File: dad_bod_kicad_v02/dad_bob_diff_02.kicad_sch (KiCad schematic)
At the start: 68 parts

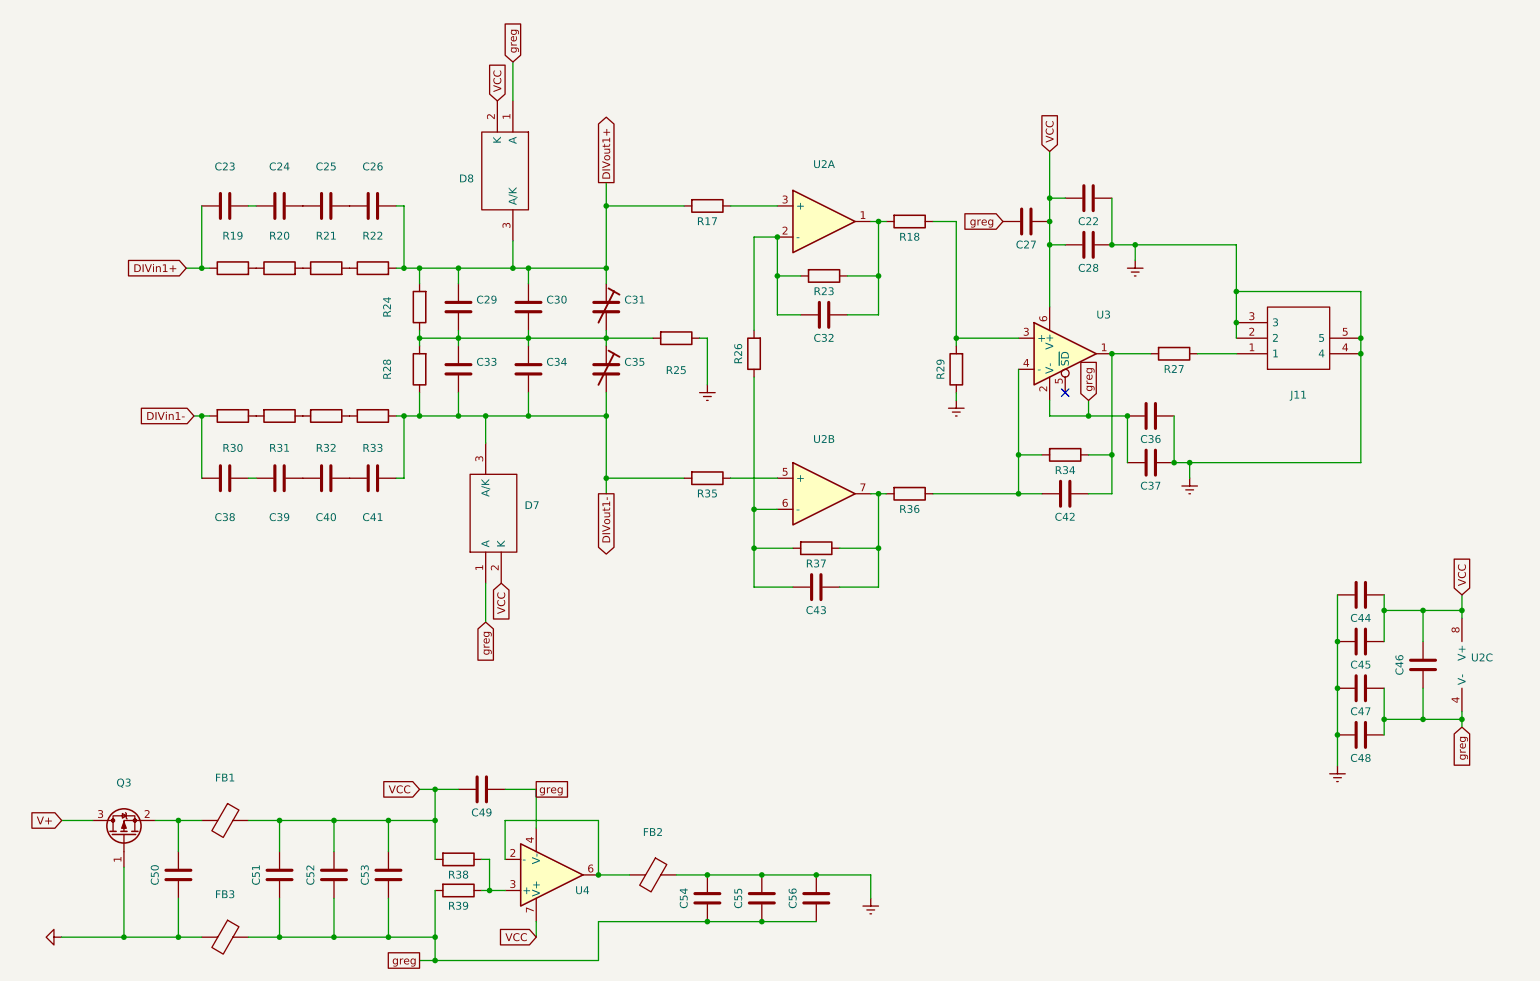
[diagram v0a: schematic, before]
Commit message: Added BOMs & db_standalone order
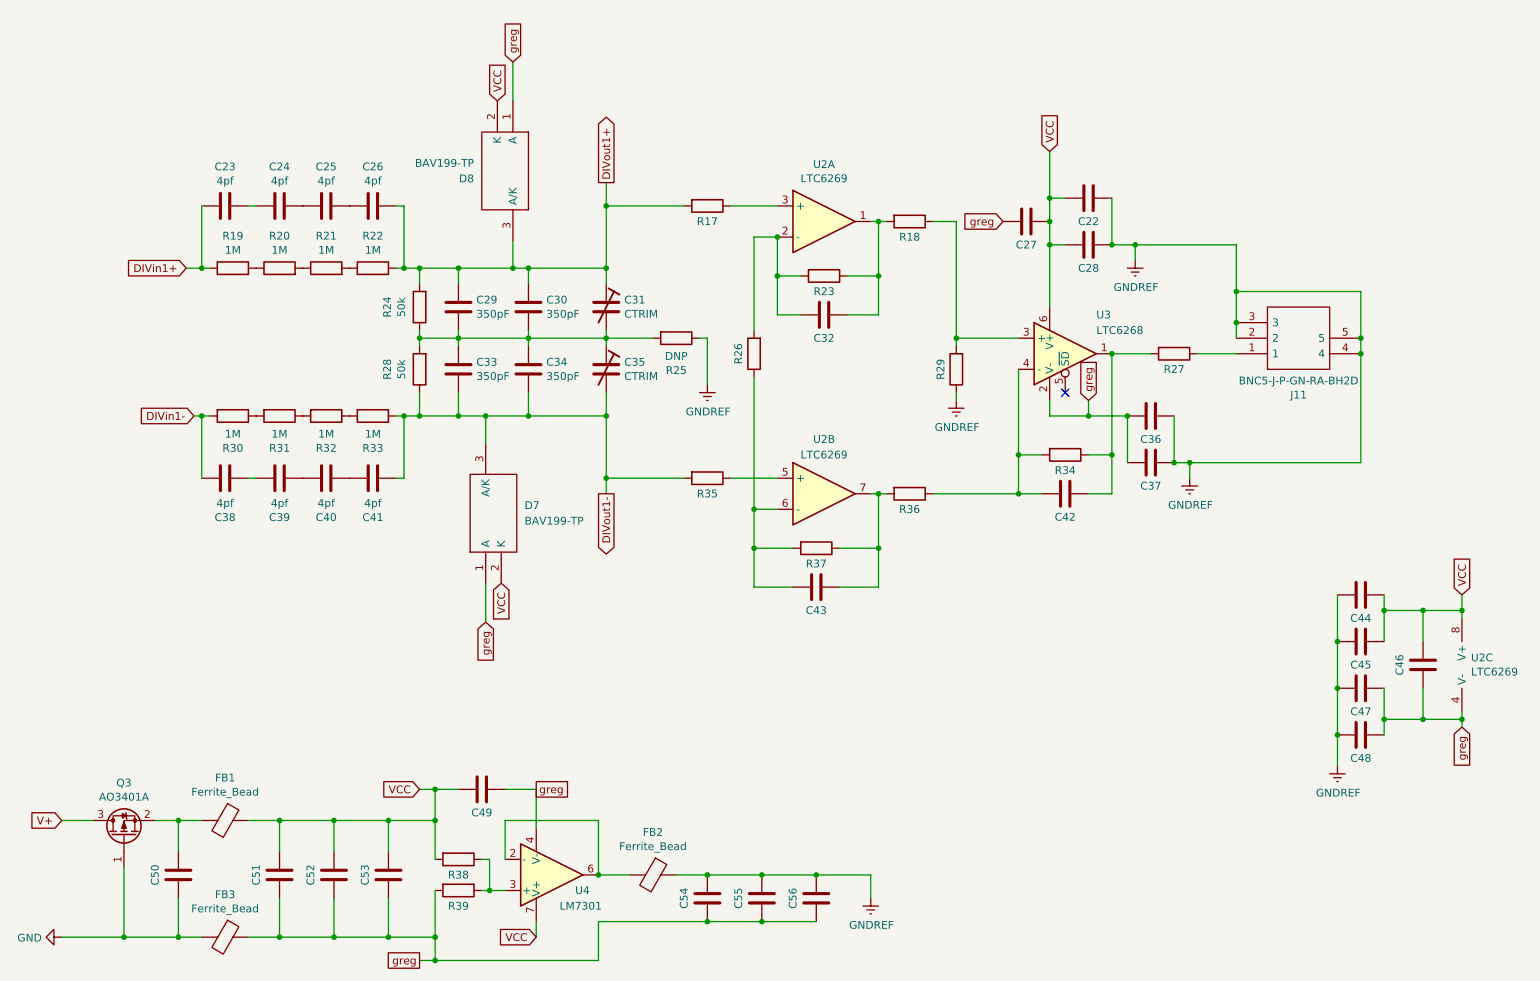
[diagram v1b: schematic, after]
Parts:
- C22, C27, C28, C32, C36, C37, C42, C43, C44, C45, C46, C47, C48, C49, C50, C51, C52, C53, C54, C55, C56: value (none) -> ~; footprint (none) -> Capacitor_SMD:C_0805_2012Metric_Pad1.15x1.40mm_HandSolder
- C23, C24, C25, C26, C38, C39, C40, C41: value (none) -> 4pf; footprint (none) -> Capacitor_SMD:C_0805_2012Metric_Pad1.15x1.40mm_HandSolder
- C29, C30, C33, C34: value (none) -> 350pF; footprint (none) -> Capacitor_SMD:C_0805_2012Metric_Pad1.15x1.40mm_HandSolder
- C31, C35: value (none) -> CTRIM; footprint (none) -> Capacitor_SMD:C_Trimmer_Voltronics_JQ
- D7, D8: value (none) -> BAV199-TP; footprint (none) -> kyuditsky_kicad:bav199_tp_SOT95P237X125-3N
- FB1, FB2, FB3: value (none) -> Ferrite_Bead; footprint (none) -> Resistor_SMD:R_0805_2012Metric_Pad1.20x1.40mm_HandSolder
- J11: value (none) -> BNC5-J-P-GN-RA-BH2D; footprint (none) -> BNC5-J-P-GN-RA-BH2D_kicad:BNC5JPGNRABH2D
- Q3: value (none) -> AO3401A; footprint (none) -> Package_TO_SOT_SMD:SOT-23
- R17, R18, R23, R26, R27, R29, R34, R35, R36, R37, R38, R39: value (none) -> ~; footprint (none) -> Resistor_SMD:R_0805_2012Metric_Pad1.15x1.40mm_HandSolder
- R19, R20, R21, R22, R30, R31, R32, R33: value (none) -> 1M; footprint (none) -> Resistor_SMD:R_0805_2012Metric_Pad1.15x1.40mm_HandSolder
- R24, R28: value (none) -> 50k; footprint (none) -> Resistor_SMD:R_0805_2012Metric_Pad1.15x1.40mm_HandSolder
- R25: value (none) -> DNP; footprint (none) -> Resistor_SMD:R_0805_2012Metric_Pad1.15x1.40mm_HandSolder
- U2: value (none) -> LTC6269; footprint (none) -> LTC6269:SOP65P490X110-9N
- U3: value (none) -> LTC6268; footprint (none) -> LTC6268IS6-10#TRMPBF:SOT95P280X100-6N
- U4: value (none) -> LM7301; footprint (none) -> LTC6269:SOP65P490X110-9N

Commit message: Added buds_diffprobe_spice and waveforms psu testing
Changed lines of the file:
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@@
   (junction (at 86.36 163.83) (diameter 0) (color 0 0 0 0)
+  )
+  (junction (at 110.49 158.75) (diameter 0) (color 0 0 0 0)
   )
   (junction (at 121.92 73.66) (diameter 0) (color 0 0 0 0)
@@
   )
   (wire (pts (xy 255.27 129.54) (xy 261.62 129.54))
+    (stroke (width 0) (type default) (color 0 0 0 0))
+  )
+  (wire (pts (xy 110.49 158.75) (xy 114.3 158.75))
     (stroke (width 0) (type default) (color 0 0 0 0))
   )
@@
     )
   )
-  (global_label "greg" (shape passive) (at 110.49 158.75 0) (fields_autoplaced)
+  (global_label "greg" (shape passive) (at 114.3 158.75 0) (fields_autoplaced)
     (effects (font (size 1.27 1.27)) (justify left))
-    (property "Intersheet References" "${INTERSHEET_REFS}" (id 0) (at 0 0 0)
-      (effects (font (size 1.27 1.27)) hide)
-    )
+    (property "Intersheet References" "${INTERSHEET_REFS}" (id 0) (at 3.81 0 0)
+      (effects (font (size 1.27 1.27)) hide)
+    )
